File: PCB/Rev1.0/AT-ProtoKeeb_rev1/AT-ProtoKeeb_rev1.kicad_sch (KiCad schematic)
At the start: 107 parts, among them J1 USB4105-GF-A, U1 Raspberry Pi Pico, U2 TXB0102DCU, U3 USBLC6-2SC6

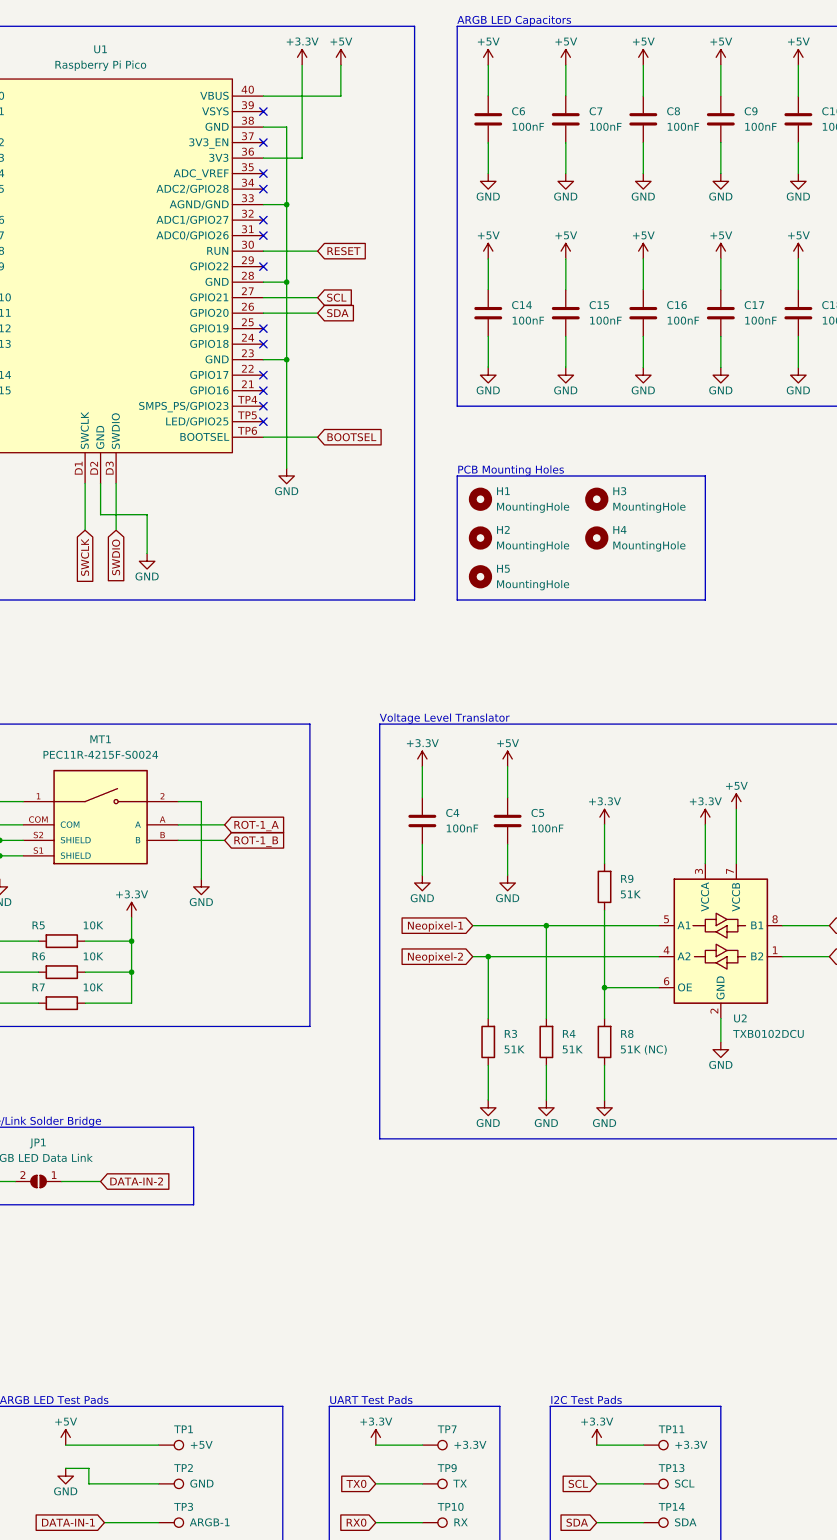
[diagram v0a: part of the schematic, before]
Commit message: Added Assembly Instructions
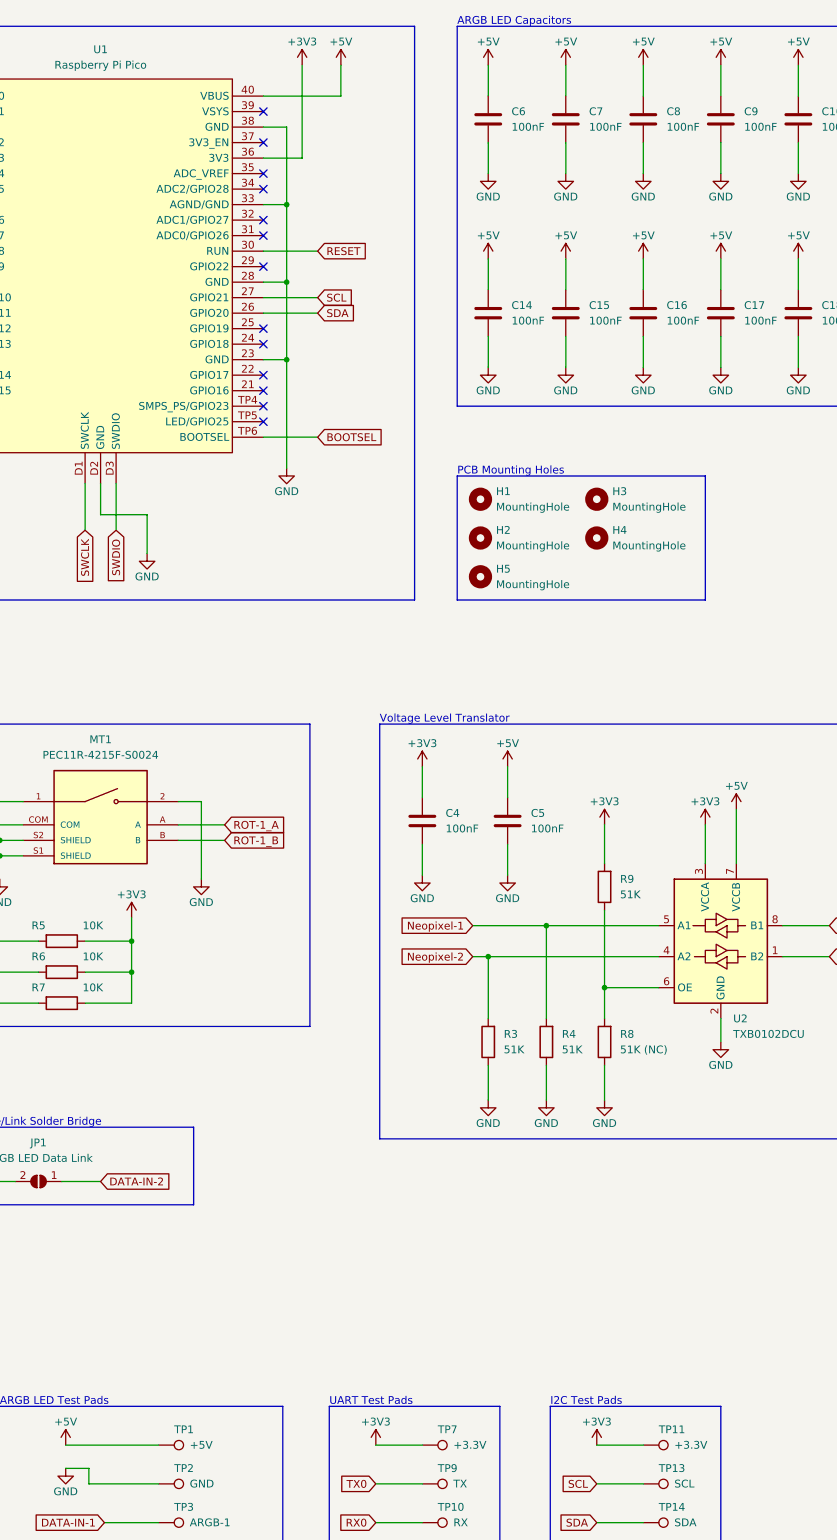
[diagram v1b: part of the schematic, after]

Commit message: minor changes and improvements in the Protokeeb Rev1 PCB files
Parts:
- removed MT1: PEC11R-4215F-S0024, PEC11R-4215F-S0024:XDCR_PEC11R-4215F-S0024, symbol RPi_Pico_SMD:PEC11R-4215F-S0024
- removed U2: TXB0102DCU, Package_SO:VSSOP-8_2.4x2.1mm_P0.5mm, symbol Logic_LevelTranslator:TXB0102DCU
- removed U3: USBLC6-2SC6, Package_TO_SOT_SMD:SOT-23-6, symbol Power_Protection:USBLC6-2SC6
- added JP2, JP3: ARGB LED Data Link, Jumper:SolderJumper-2_P1.3mm_Open_TrianglePad1.0x1.5mm, symbol Jumper:SolderJumper_2_Open
- added MT1: PEC11R-4215F-S0024, PEC11R-4215F-S0024:XDCR_PEC11R-4215F-S0024, symbol PEC11R-4215F-S0024:PEC11R-4215F-S0024
- added U2: TXB0102DCUR, TXB0102DCUR:SOP50P310X90-8N, symbol TXB0102DCUR:TXB0102DCUR
- added U3: USBLC6-2SC6, USBLC6-2SC6:SOT95P280X145-6N, symbol USBLC6-2SC6:USBLC6-2SC6
- BTN1, BTN2: DigiKey Part Number (none) -> 39-B3U-1000PMTR-ND; LCSC Part Number (none) -> C18077679; Mouser Part Number (none) -> 653-B3U-1000PM
- C1: DigiKey Part Number (none) -> 311-1085-1-ND; LCSC Part Number (none) -> C100042; Mouser Part Number (none) -> 603-CC603KRX7R9BB103
- C10, C11, C12, C13, C14, C15, C16, C17, C18, C19, C2, C20, C21, C4, C5, C6, C7, C8, C9: DigiKey Part Number (none) -> 490-5798-1-ND; LCSC Part Number (none) -> C161115; Mouser Part Number (none) -> 81-GCJ188R71H104KA2D
- C3: DigiKey Part Number (none) -> 490-GRM188Z71C475KE21DCT-ND; LCSC Part Number (none) -> C389010; Mouser Part Number (none) -> 81-GRM188Z71C475KE1D
- D1: DigiKey Part Number (none) -> SS14CT-ND; LCSC Part Number (none) -> C83852; Mouser Part Number (none) -> 512-SS14
- D10, D11, D12, D13, D14, D15, D16, D17, D2, D3, D4, D5, D6, D7, D8, D9: DigiKey Part Number (none) -> 1N4148WSFSCT-ND; LCSC Part Number (none) -> C181133; Mouser Part Number (none) -> 512-1N4148WS
- FB1: DigiKey Part Number (none) -> 445-MPZ1608S221ATA00CT-ND; LCSC Part Number (none) -> C76815; Mouser Part Number (none) -> 810-MPZ1608S221ATA00
- J1: Description_1 (none) -> USB-C (USB TYPE-C) USB 2.0 Receptacle Connector 24 (16+8 Du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; DigiKey Part Number (none) -> 2073-USB4105-GF-ACT-ND; LCSC Part Number (none) -> C2689843; Mouser Part Number (none) -> 640-USB4105-GF-A
- LED1, LED10, LED11, LED12, LED13, LED14, LED15, LED16, LED2, LED3, LED4, LED5, LED6, LED7, LED8, LED9: DigiKey Part Number (none) -> 1528-4684-ND; LCSC Part Number (none) -> C965555; Mouser Part Number (none) -> 485-4684; Mouser Price/Stock (none) -> https://www.mouser.com/ProductDetail/Adafruit/4684?qs=DPoM0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
- R1, R2: DigiKey Part Number (none) -> 311-5.10KHRCT-ND; LCSC Part Number (none) -> C105580; Mouser Part Number (none) -> 603-RC0603FR-075K1L
- R3, R4, R8, R9: DigiKey Part Number (none) -> 311-51.0KHRCT-ND; LCSC Part Number (none) -> C107231; Mouser Part Number (none) -> 603-RC0603FR-0751KL
- R5, R6, R7: DigiKey Part Number (none) -> 311-10.0KHRCT-ND; LCSC Part Number (none) -> C98220; Mouser Part Number (none) -> 603-RC0603FR-0710KL
- S1, S10, S11, S12, S13, S14, S15, S16, S2, S3, S4, S5, S6, S7, S8, S9: DigiKey Part Number (none) -> CH160-ND; LCSC Part Number (none) -> C3316924
- U1: DigiKey Part Number (none) -> 2648-SC0915CT-ND; LCSC Part Number (none) -> C7203002; Mouser Part Number (none) -> 358-SC0915
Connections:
- net +3V3: now also U2.3 (VCCA)
- net +5V: now also U2.7 (VCCB)
- net DATA-IN-1: now also JP2.2 (B), U2.8 (B1)
- net DATA-IN-2: now also JP3.2 (B), U2.1 (B2)
- net GND: now also MT1.2, MT1.COM, MT1.S1 (SHIELD), MT1.S2 (SHIELD), U2.2 (GND), U3.2
- net Neopixel-1: now also JP2.1 (A), U2.5 (A1)
- net Neopixel-2: now also JP3.1 (A), U2.4 (A2)
- net ROT-1_A: now also MT1.A
- net ROT-1_B: now also MT1.B
- net ROT-1_SW: now also MT1.1
- net USB_DM_IN: now also U3.3
- net USB_DM_OUT: now also U3.4
- net USB_DP_IN: now also U3.1
- net USB_DP_OUT: now also U3.6
- net VBUS: now also U3.5
- net at R8.2, R9.1: now also U2.6 (OE)
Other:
- note added: "Solder Bridge Jumpers"
- note removed: "ARGB LED Data Share/Link Solder Bridge"
- moved on the sheet: C1, C3, D1, FB1, JP1, R1, R3, R5, TP1, TP10, TP11, TP12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
